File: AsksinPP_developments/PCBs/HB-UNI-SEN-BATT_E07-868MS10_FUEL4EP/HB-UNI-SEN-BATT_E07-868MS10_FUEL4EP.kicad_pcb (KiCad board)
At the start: 2 copper layers, 75 x 75 mm, 30 parts, among them J1 Conn_01x02, J10 charge, J11 ePaper connector, J2 Conn_01x02, J3 Conn_01x02, J4 Conn_01x02, J5 ISP Programmer, J6 Conn_01x04, J7 Conn_01x04, J8 Conn_01x04, J9 Conn_01x04, Q1 IRLU024N, SW1 config button

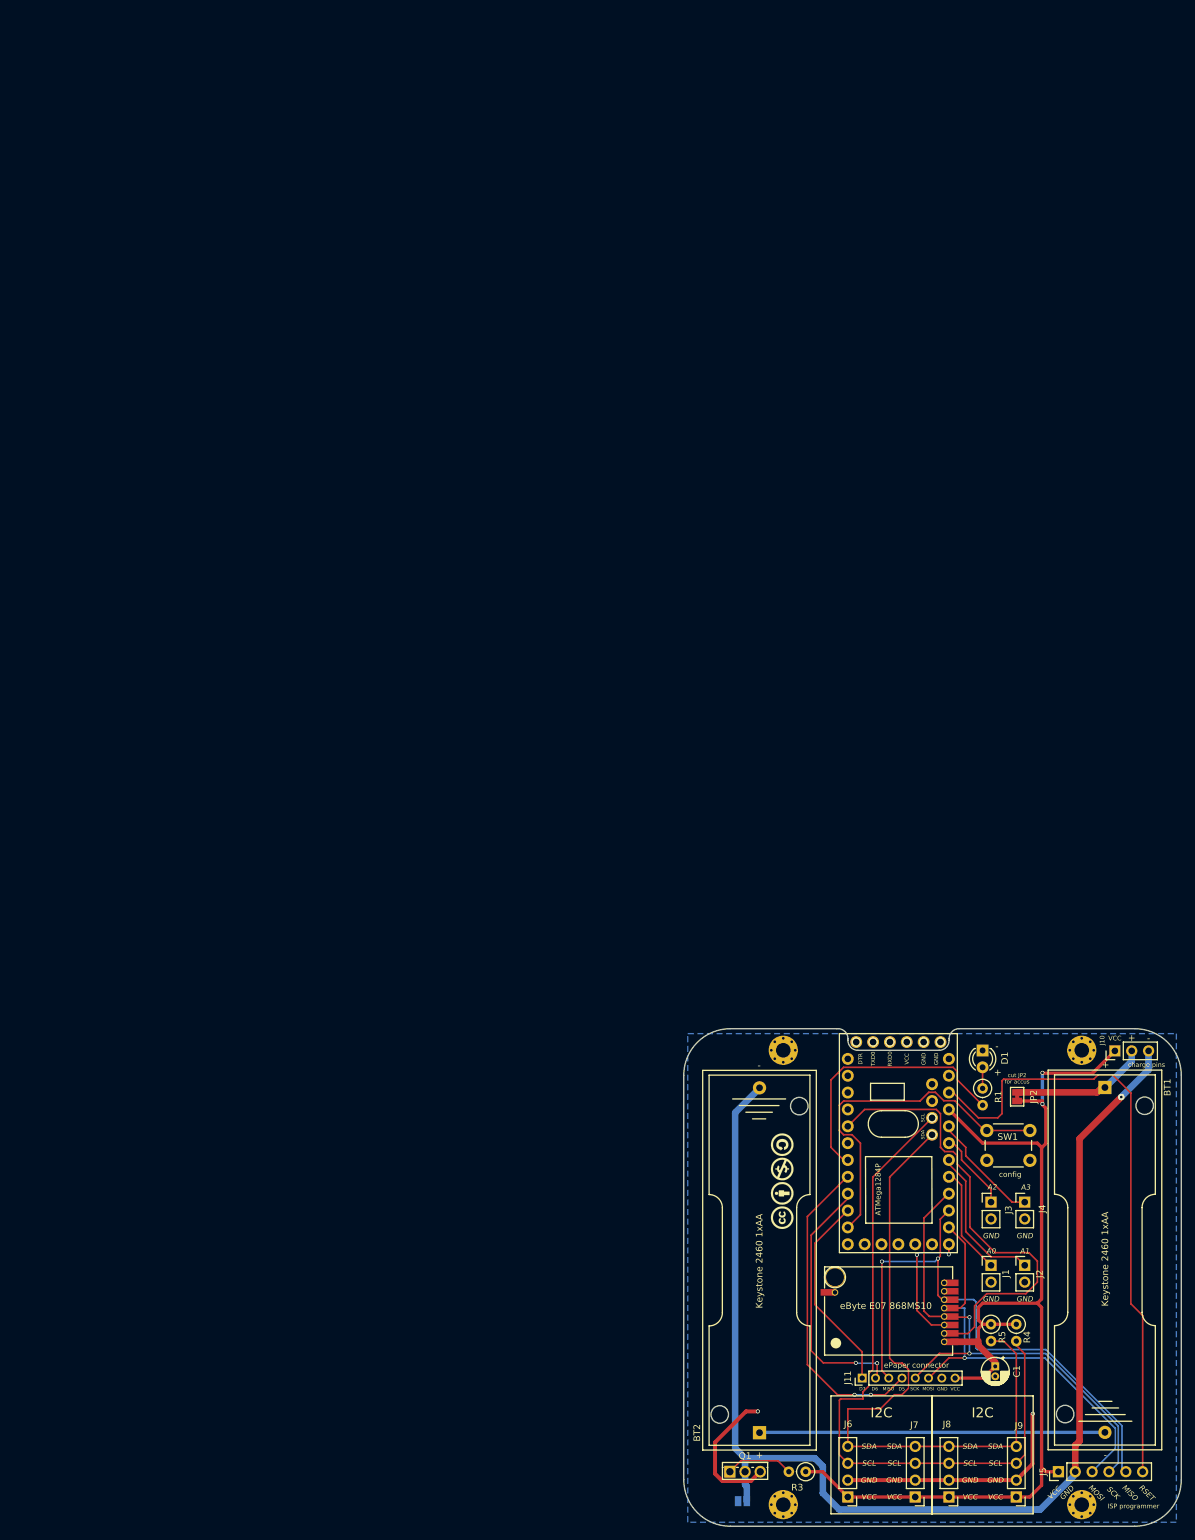
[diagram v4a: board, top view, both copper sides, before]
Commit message: PCBs: Fixes to ensure a proper production at JLCPCB, e.g. corrections of origins, rotations of assembled ICs etc.
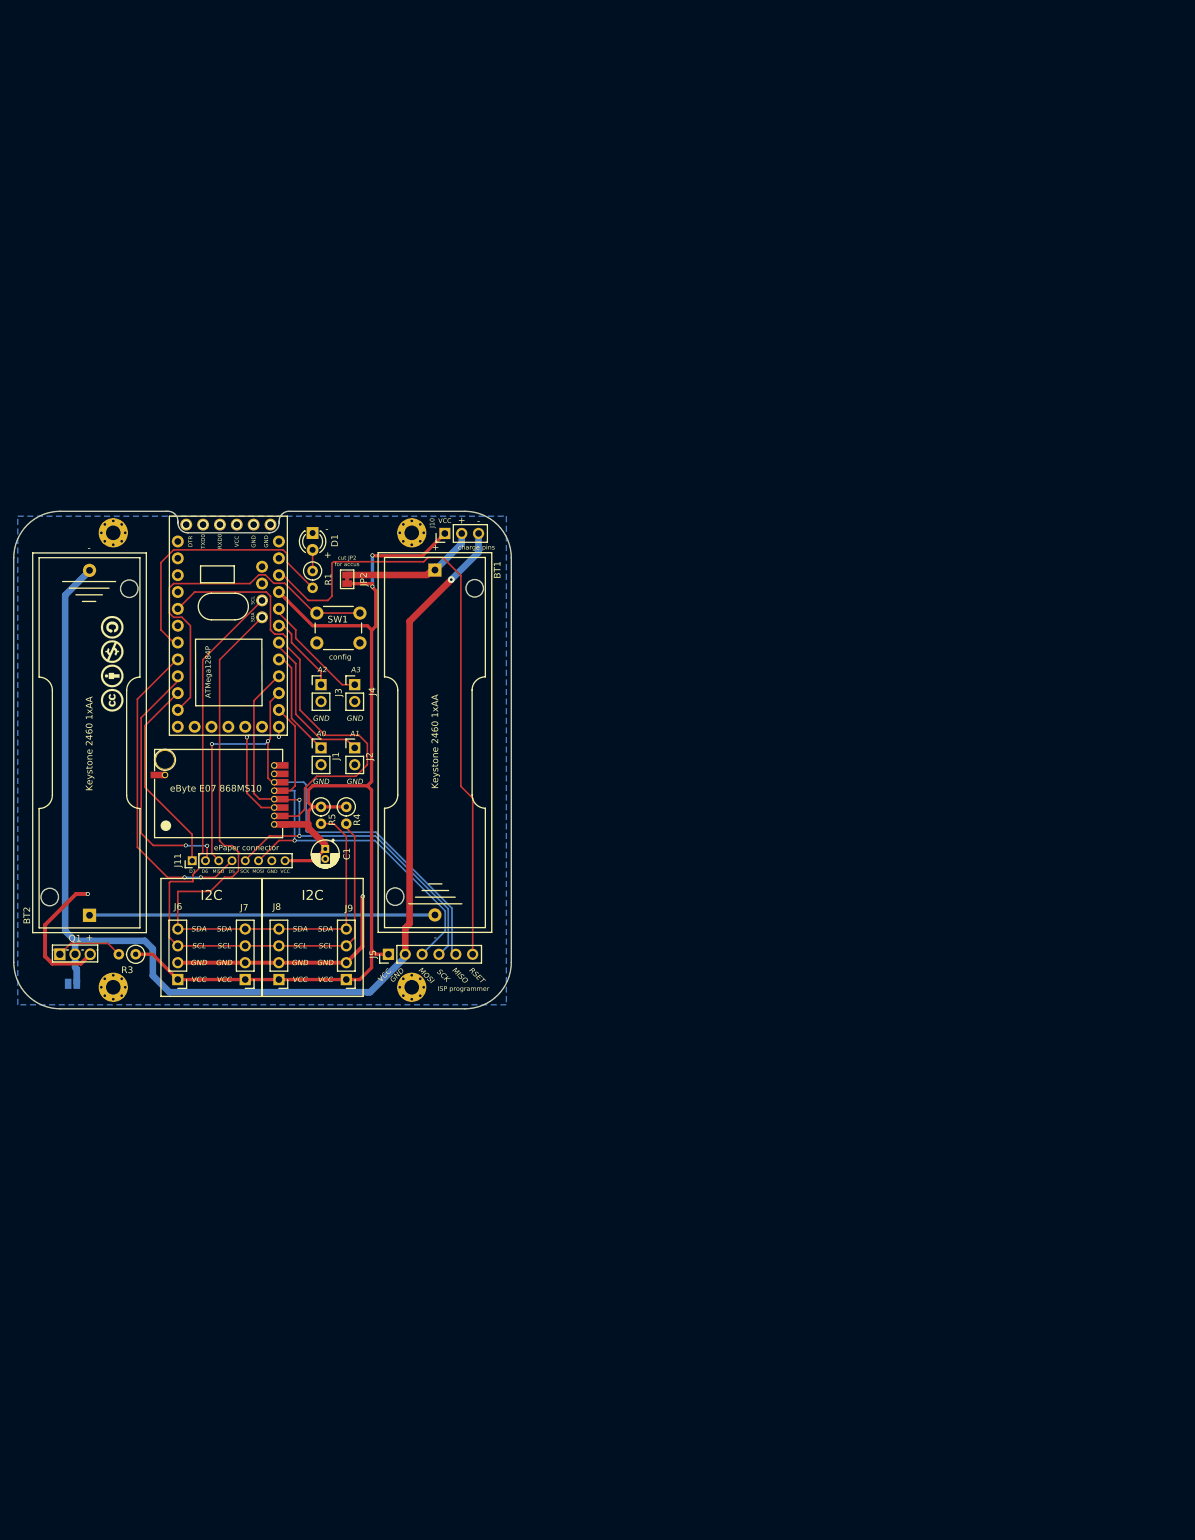
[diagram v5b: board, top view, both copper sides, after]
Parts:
- moved C1 127.6 mm to (47.0, 50.9)
- moved D1 127.6 mm to (45.0, 3.28)
- moved R1 127.6 mm to (45.0, 8.99)
- moved BT1 127.6 mm to (63.5, 8.86)
- moved BT2 127.6 mm to (11.4, 60.9)
- moved H1 127.6 mm to (15.0, 3.25)
- moved H2 127.6 mm to (60.0, 3.25)
- moved H3 127.6 mm to (15.0, 71.8)
- moved H4 127.6 mm to (60.0, 71.8)
- moved J1 127.6 mm to (46.3, 35.7)
- moved J10 127.6 mm to (65.0, 3.34)
- moved J11 127.6 mm to (26.9, 52.7)
- moved J2 127.6 mm to (51.4, 35.7)
- moved J3 127.6 mm to (46.3, 26.1)
- moved J4 127.6 mm to (51.4, 26.1)
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
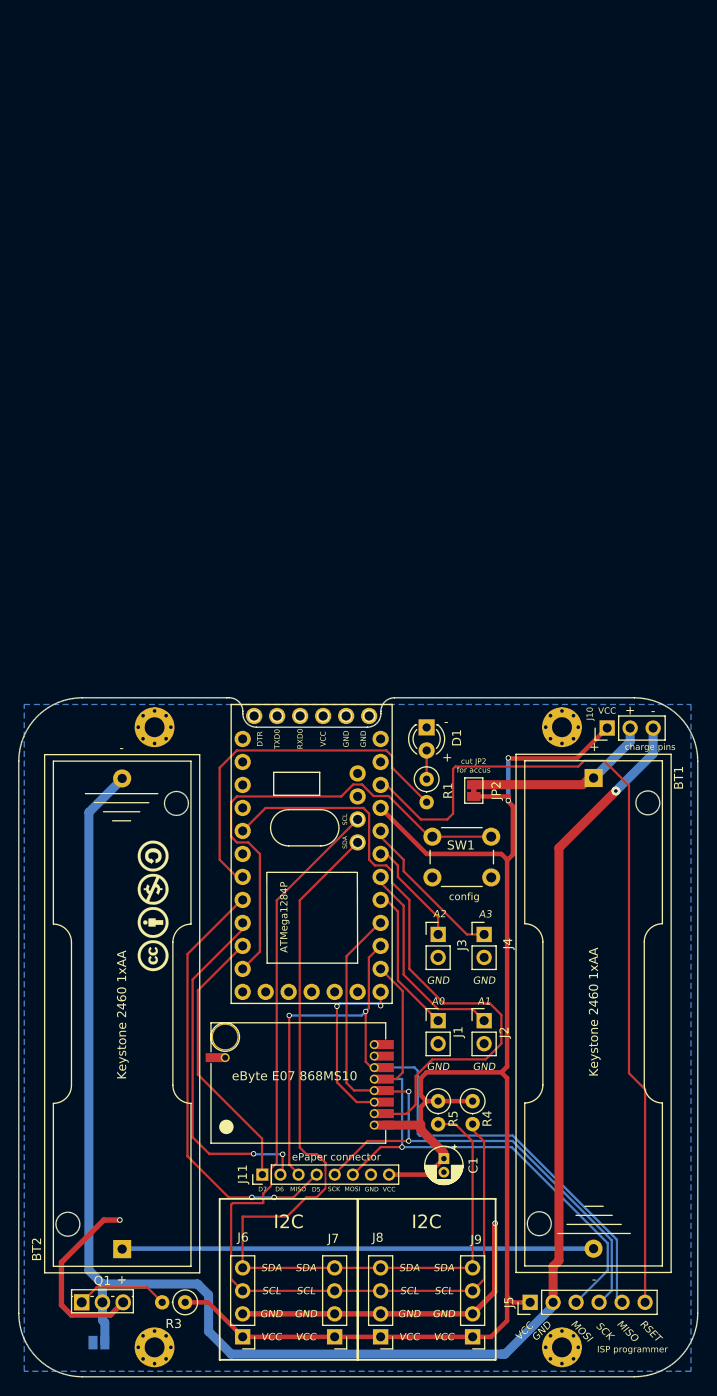
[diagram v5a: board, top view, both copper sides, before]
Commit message: PCBs: moved origin to lower left corner in order to fit to JLCPCB's scheme
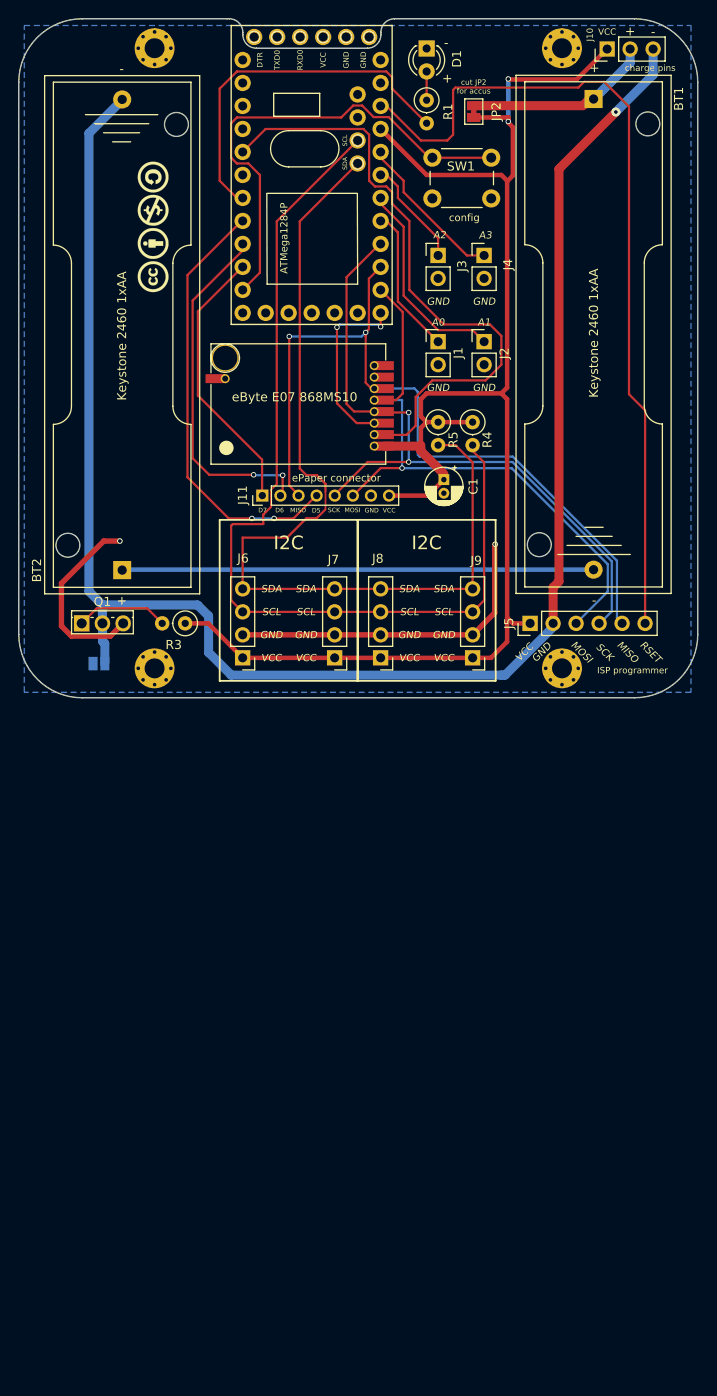
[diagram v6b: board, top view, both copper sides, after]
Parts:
- moved BT1 75.0 mm to (63.5, -66.1)
- moved BT2 75.0 mm to (11.4, -14.1)
- moved C1 75.0 mm to (47.0, -24.1)
- moved D1 75.0 mm to (45.0, -71.7)
- moved H1 75.0 mm to (15.0, -71.8)
- moved H2 75.0 mm to (60.0, -71.8)
- moved H3 75.0 mm to (15.0, -3.25)
- moved H4 75.0 mm to (60.0, -3.25)
- moved J1 75.0 mm to (46.3, -39.3)
- moved J10 75.0 mm to (65.0, -71.7)
- moved J11 75.0 mm to (26.9, -22.3)
- moved J2 75.0 mm to (51.4, -39.3)
- moved J3 75.0 mm to (46.3, -48.9)
- moved J4 75.0 mm to (51.4, -48.9)
- moved J5 75.0 mm to (56.5, -8.22)
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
